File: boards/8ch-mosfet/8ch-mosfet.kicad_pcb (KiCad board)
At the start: 2 copper layers, 184.5 x 137 mm, 150 parts, among them J1 N2K, J10 Screw_Terminal_01x02, J11 Screw_Terminal_01x02, J12 Screw_Terminal_01x02, J2 I2C, J3 Screw_Terminal_01x08, J5 Screw_Terminal_01x02, J6 Screw_Terminal_01x02, J7 Screw_Terminal_01x02, J8 Screw_Terminal_01x02, J9 Screw_Terminal_01x02, M1 Fan_4pin, M2 Fan_4pin, Q1 2N7002, Q10 IRF4905, Q11 2N7002, Q12 IRF4905, Q13 2N7002, Q14 IRF4905, Q15 2N7002, Q16 IRF4905, Q2 IRF4905, Q3 2N7002, Q4 IRF4905, Q5 2N7002, Q6 IRF4905, Q7 2N7002, Q8 IRF4905, Q9 2N7002, U1 ESP32-DEVKITC, U10 ACS725xLCTR-20AU, U11 ACS725xLCTR-20AU, U12 ACS725xLCTR-20AU, U2 MCP3208, U3 R-78B3.3-2.0, U4 MCP3221A0T, U5 ACS725xLCTR-20AU, U6 ACS725xLCTR-20AU, U7 ACS725xLCTR-20AU, U8 ACS725xLCTR-20AU, U9 ACS725xLCTR-20AU

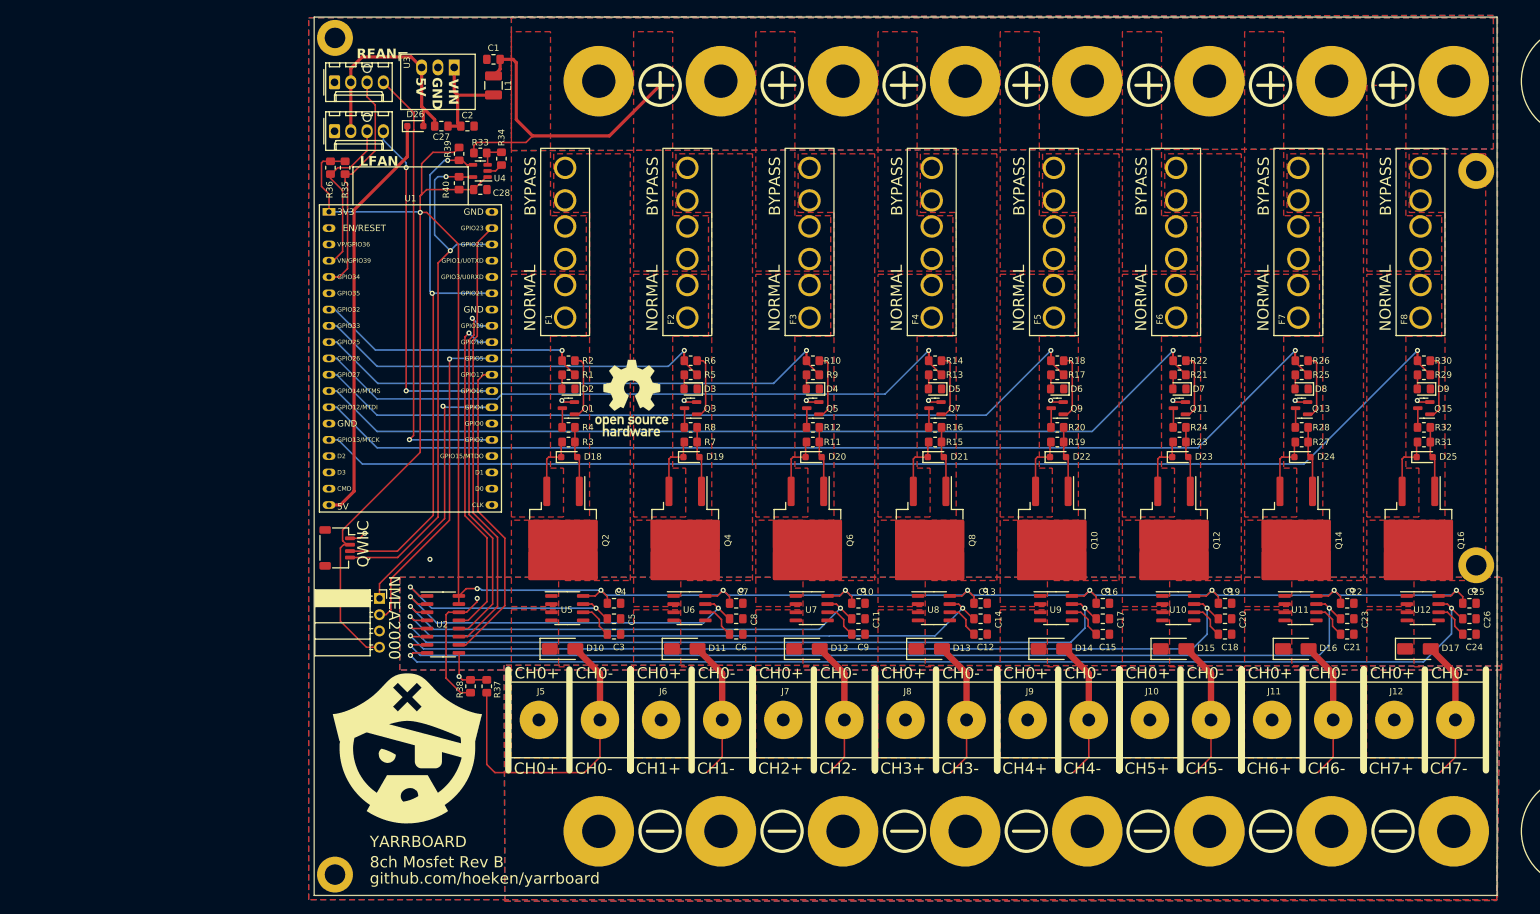
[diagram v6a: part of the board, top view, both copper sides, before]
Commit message: upgraded the i2c/serial connectors + power based on the sailor hat schematic
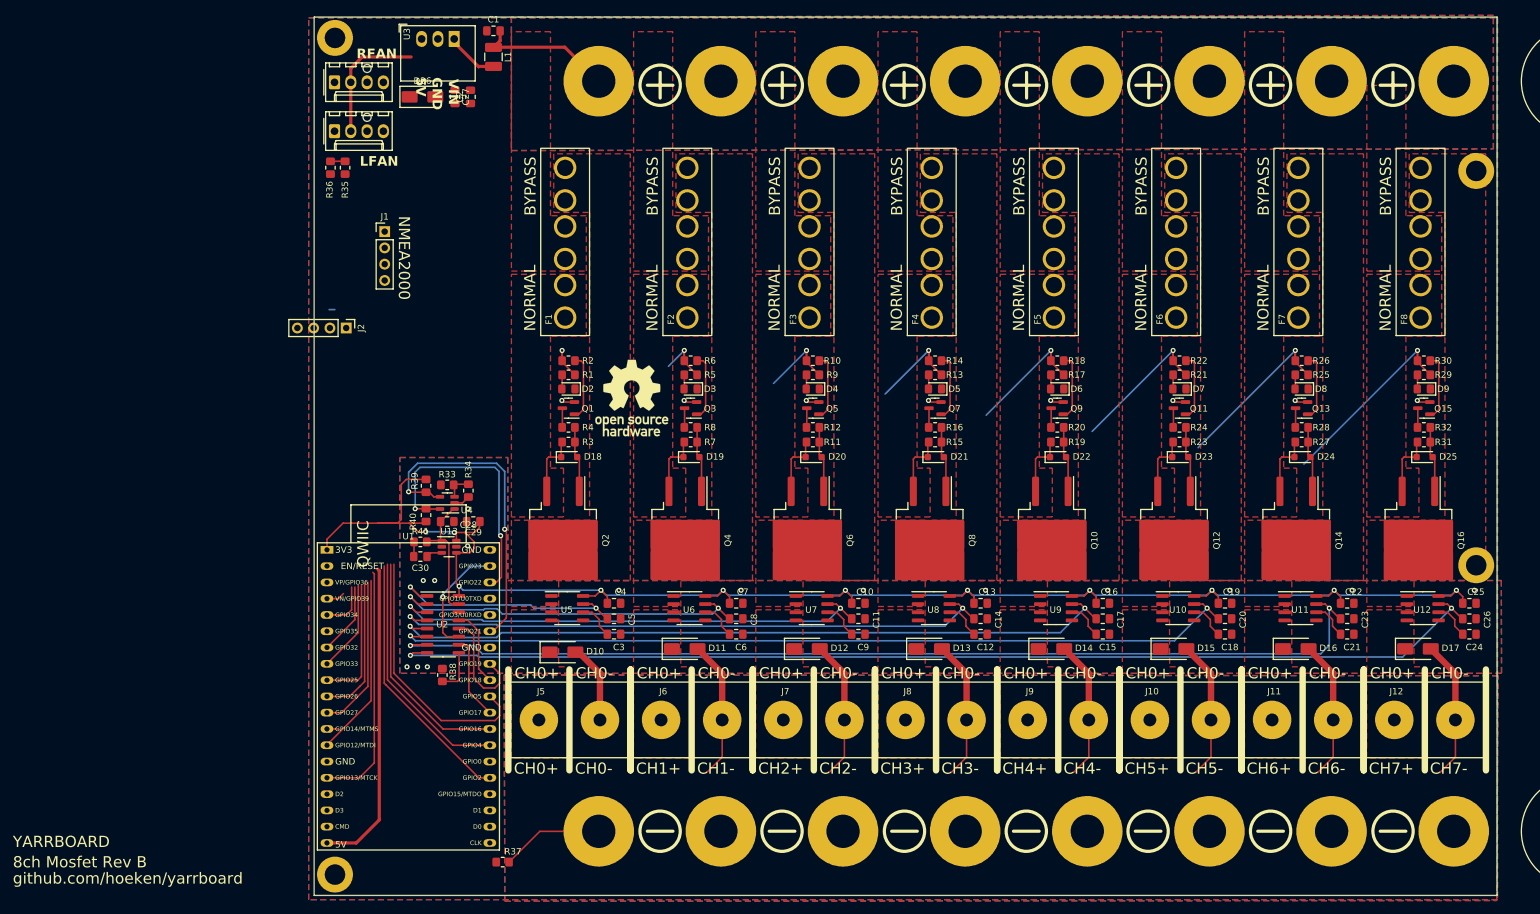
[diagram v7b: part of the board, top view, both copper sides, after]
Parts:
- removed the REF** at (14.4, 115.1)
- added C29: 100nF, Capacitor_SMD:C_0805_2012Metric_Pad1.18x1.45mm_HandSolder, F.Cu at (24.8, 78.7)
- added C30: 100nF, Capacitor_SMD:C_0805_2012Metric_Pad1.18x1.45mm_HandSolder, F.Cu at (16.6, 84.1)
- added R41: 10k, Resistor_SMD:R_0805_2012Metric_Pad1.20x1.40mm_HandSolder, F.Cu at (16.6, 81.9)
- added U13: MCP1502, Package_TO_SOT_SMD:SOT-23-6, F.Cu at (21.0, 82.6)
- C28: value 1nF -> 100nF
- D26: value CMHSH5-2L -> SX33L; footprint Diode_SMD:D_SOD-323_HandSoldering -> Diode_SMD:D_SMA
- J1: footprint Connector_PinSocket_2.54mm:PinSocket_1x04_P2.54mm_Horizontal -> Connector_PinHeader_2.54mm:PinHeader_1x04_P2.54mm_Vertical
- J2: footprint Connector_JST:JST_SH_SM04B-SRSS-TB_1x04-1MP_P1.00mm_Horizontal -> Connector_PinHeader_2.54mm:PinHeader_1x04_P2.54mm_Vertical
- U3: value R-78B3.3-2.0 -> R-78K5.0-1.0
- moved J1 57.2 mm to (11.0, 33.5)
- moved U1 52.7 mm to (2.00, 83.1)
- moved C28 52.0 mm to (20.8, 78.7)
- moved R33 52.0 mm to (20.8, 73.0)
- moved R34 52.0 mm to (24.1, 73.9)
- moved R39 52.0 mm to (17.5, 73.1)
- moved R40 52.0 mm to (17.5, 77.7)
- moved U4 52.0 mm to (20.8, 75.8)
- moved J2 34.3 mm to (5.00, 48.5)
- moved R37 27.5 mm to (29.4, 131.8), turned to 0 degrees
- moved C27 5.04 mm to (22.0, 12.4), turned to -90 degrees
- moved R38 4.72 mm to (20.0, 102.6), turned to -90 degrees
- moved D26 4.70 mm to (16.9, 12.4)
- moved C2 4.59 mm to (24.4, 12.4), turned to 90 degrees
- moved C1 4.45 mm to (28.0, 2.15)
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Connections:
- C28 pad 1: +3.3V -> REF_3V3
- C28 pad 2: GNDD -> GNDA
- J2 pad 1: GNDD -> SDA
- J2 pad 2: +3.3V -> SCL
- J2 pad 3: SDA -> GNDD
- J2 pad 4: SCL -> +3.3V
- R34 pad 1: GNDD -> GNDA
- U2 pad 15: +3.3V -> REF_3V3
- U4 pad 1: +3.3V -> REF_3V3
- U4 pad 2: GNDD -> GNDA
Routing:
- net +3.3V: track 400.8 -> 266.9 mm, vias 10 -> 11
- net /PWM5: track 145.7 -> 25.9 mm
- net /PWM7: track 184.9 -> 69.4 mm
- net /PWM6: track 165.8 -> 56.2 mm
- net /PWM4: track 125.6 -> 44.8 mm
- net /PWM3: track 105.5 -> 37.9 mm
- net /PWM2: track 85.5 -> 33.3 mm
- net Net-(U1-GPIO23): track 69.8 -> 17.9 mm, vias 0 -> 1
- net SCL: track 83.8 -> 42.0 mm
- net /PWM1: track 65.3 -> 24.0 mm
- net Net-(U1-GPIO18): track 53.3 -> 12.2 mm, vias 1 -> 0
- net Net-(U1-GPIO19): track 56.9 -> 18.2 mm, vias 1 -> 0
- net Net-(U1-GPIO17): track 49.1 -> 13.3 mm
- net SDA: track 85.9 -> 50.7 mm
- net +24V: track 52.3 -> 21.6 mm
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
